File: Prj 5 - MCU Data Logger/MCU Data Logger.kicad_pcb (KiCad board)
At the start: 2 copper layers, 0 parts

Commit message: setup layout parameters
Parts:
- added BT1: Battery, Connector_PinHeader_2.54mm:PinHeader_1x02_P2.54mm_Vertical, F.Cu at (23.1, 45.1)
- added C1: 0.1u, Capacitor_SMD:C_0805_2012Metric, F.Cu at (44.8, 34.9)
- added C2: 0.1u, Capacitor_SMD:C_0805_2012Metric, F.Cu at (44.8, 37.9)
- added C3: 100n, Capacitor_SMD:C_0805_2012Metric, F.Cu at (44.8, 40.9)
- added C4: 22p, Capacitor_SMD:C_0805_2012Metric, F.Cu at (44.8, 43.9)
- added C5: 22p, Capacitor_SMD:C_0805_2012Metric, F.Cu at (44.8, 46.9)
- added D1: LED, LED_SMD:LED_0805_2012Metric, F.Cu at (49.3, 34.9)
- added D2: LED, LED_SMD:LED_0805_2012Metric, F.Cu at (49.3, 37.9)
- added H1: MountingHole, MountingHole:MountingHole_2.1mm, F.Cu at (23.6, 22.7)
- added H2: MountingHole, MountingHole:MountingHole_2.1mm, F.Cu at (23.6, 28.4)
- added H3: MountingHole, MountingHole:MountingHole_2.1mm, F.Cu at (23.6, 34.2)
- added H4: MountingHole, MountingHole:MountingHole_2.1mm, F.Cu at (23.6, 39.9)
- added J1: Conn_01x04_Pin, Connector_PinHeader_2.54mm:PinHeader_1x04_P2.54mm_Vertical, F.Cu at (60.4, 22.1)
- added J2: Conn_01x09_Pin, Connector_PinHeader_2.54mm:PinHeader_1x09_P2.54mm_Vertical, F.Cu at (55.8, 22.1)
- added J3: Conn_01x04_Pin, Connector_PinHeader_2.54mm:PinHeader_1x04_P2.54mm_Vertical, F.Cu at (65.1, 22.1)
- added J4: Conn_02x03_Odd_Even, Connector_PinHeader_2.54mm:PinHeader_2x03_P2.54mm_Vertical, F.Cu at (60.4, 34.4)
- added R1: 10k, Resistor_SMD:R_0805_2012Metric, F.Cu at (28.7, 21.3)
- added R2: 10k, Resistor_SMD:R_0805_2012Metric, F.Cu at (28.7, 24.2)
- added R3: 4.7K, Resistor_SMD:R_0805_2012Metric, F.Cu at (28.7, 27.2)
- added R4: 4.7K, Resistor_SMD:R_0805_2012Metric, F.Cu at (28.7, 30.1)
- added R5: 10K, Resistor_SMD:R_0805_2012Metric, F.Cu at (28.7, 33.1)
- added R6: 330R, Resistor_SMD:R_0805_2012Metric, F.Cu at (28.7, 36.0)
- added R7: 330R, Resistor_SMD:R_0805_2012Metric, F.Cu at (28.7, 39.0)
- added U1: 24LC1025, Package_SO:SOIC-8_5.23x5.23mm_P1.27mm, F.Cu at (36.1, 23.2)
- added U2: DS1337S+, #download:SOIC127P600X175-8N, F.Cu at (36.1, 48.3)
- added U3: 24LC1025, Package_SO:SOIC-8_5.23x5.23mm_P1.27mm, F.Cu at (36.1, 30.0)
- added U4: ATmega328P, Package_QFP:TQFP-32_7x7mm_P0.8mm, F.Cu at (36.7, 39.2)
- added Y1: 32.768KHz, Crystal:Crystal_SMD_5032-2Pin_5.0x3.2mm, F.Cu at (44.9, 22.2)
- added Y2: 16MHz, Crystal:Crystal_SMD_5032-2Pin_5.0x3.2mm, F.Cu at (44.9, 27.1)

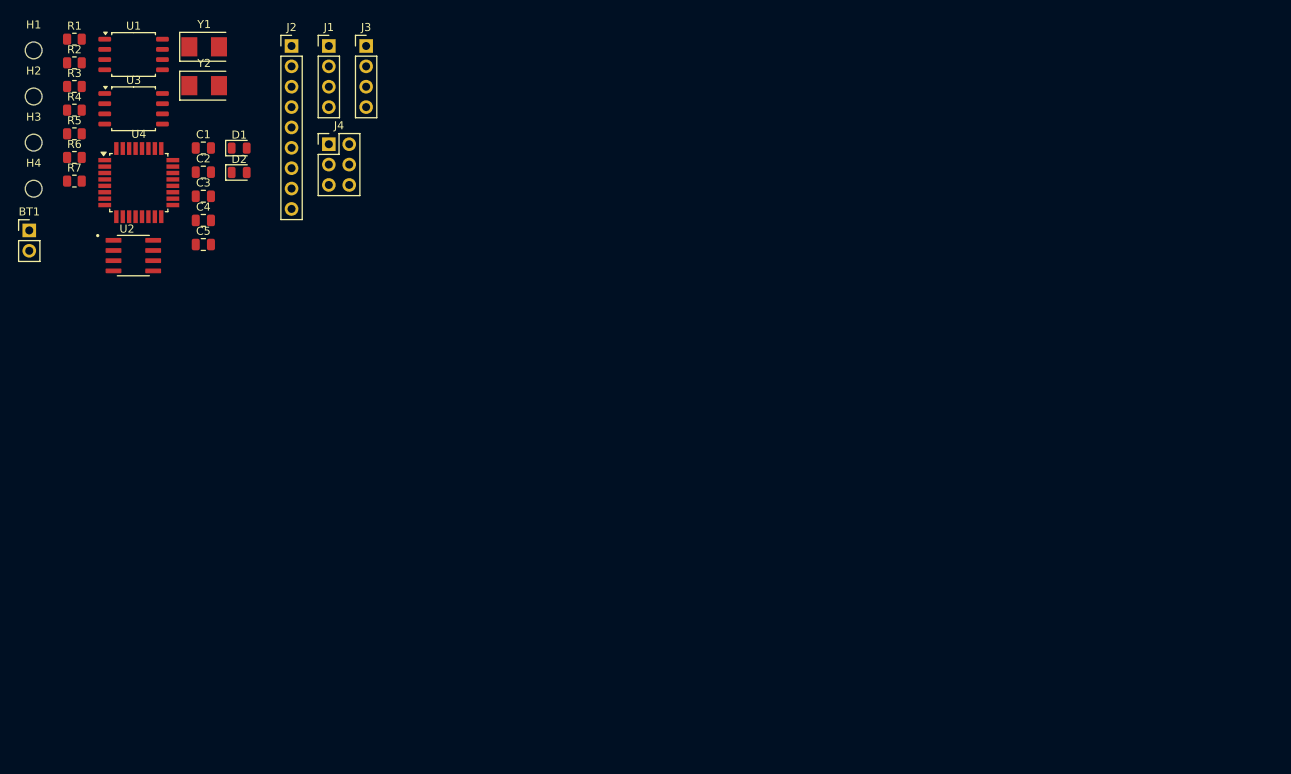
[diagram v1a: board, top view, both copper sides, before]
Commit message: distributed components and initial layout
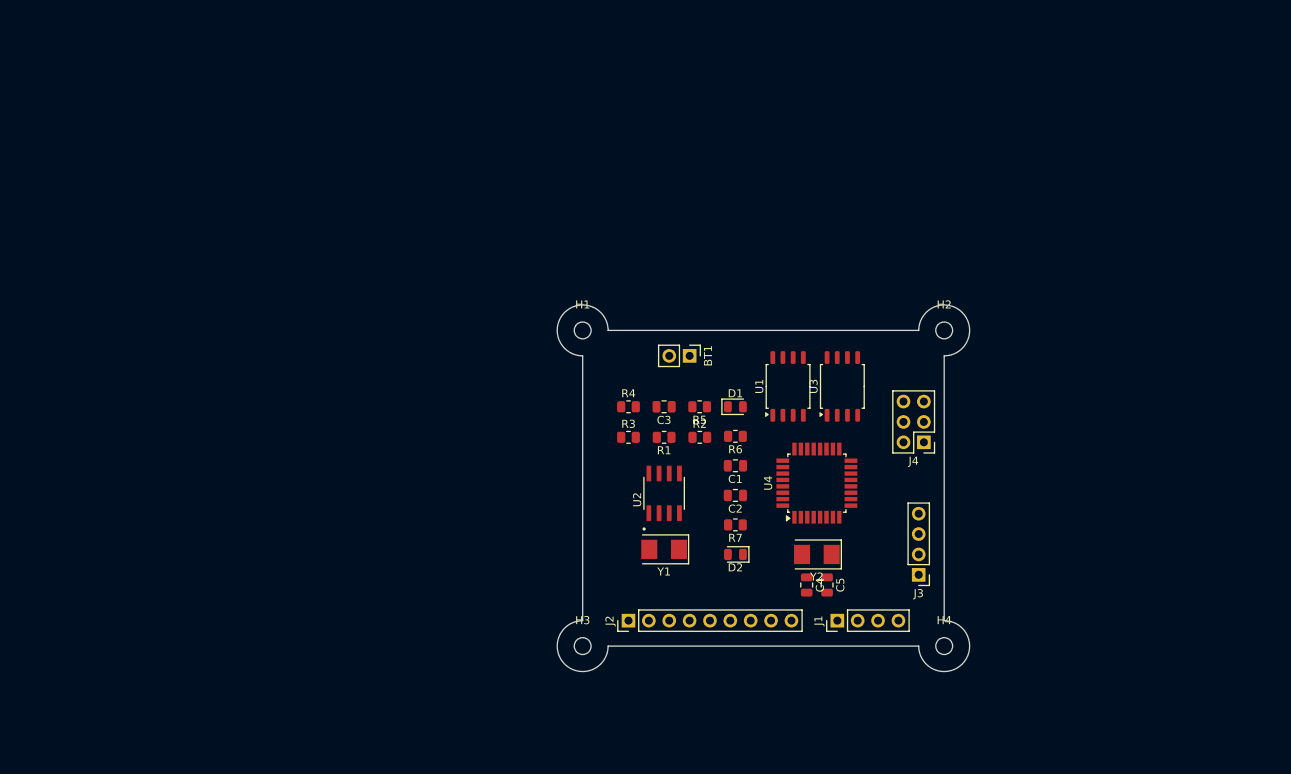
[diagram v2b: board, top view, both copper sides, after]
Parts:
- moved H4 127.1 mm to (137.2, 97.0)
- moved H2 117.2 mm to (137.2, 57.6)
- moved Y2 96.2 mm to (121.3, 85.5), turned to 180 degrees
- moved J1 95.7 mm to (123.9, 93.8), turned to 90 degrees
- moved J3 95.4 mm to (134.0, 88.1), turned to 180 degrees
- moved U3 94.9 mm to (124.5, 64.6), turned to 90 degrees
- moved R7 92.9 mm to (111.1, 81.9), turned to 180 degrees
- moved H3 92.9 mm to (92.1, 97.0)
- moved U4 92.5 mm to (121.3, 76.7), turned to 90 degrees
- moved U1 91.5 mm to (117.7, 64.6), turned to 90 degrees
- moved R2 90.9 mm to (106.7, 70.9)
- moved R6 89.5 mm to (111.1, 70.8), turned to 180 degrees
- moved R1 88.7 mm to (102.3, 70.9), turned to 180 degrees
- moved C5 88.6 mm to (122.6, 89.3), turned to -90 degrees
- moved C4 87.9 mm to (120.0, 89.3), turned to -90 degrees
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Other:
- board outline added: 51.4 x 45.7 mm

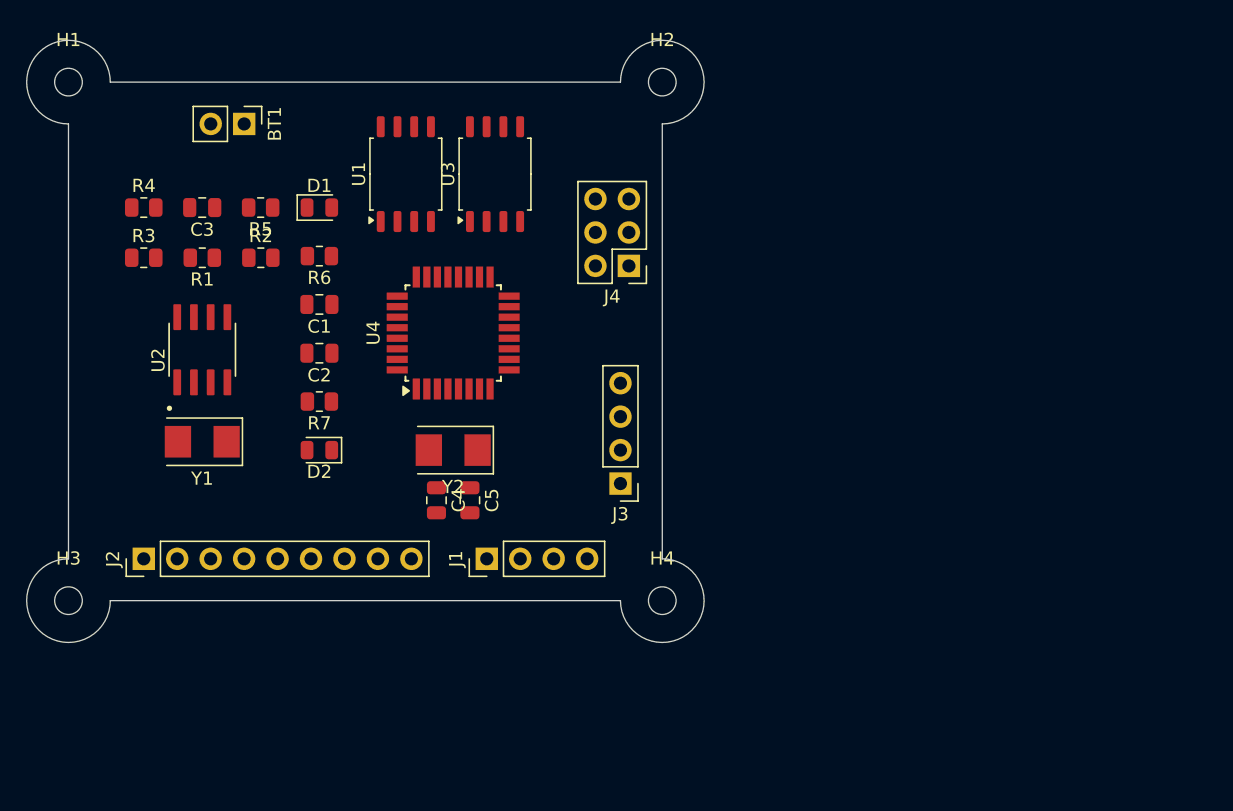
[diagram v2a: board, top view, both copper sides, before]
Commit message: Pausing, need fix on schecmatics
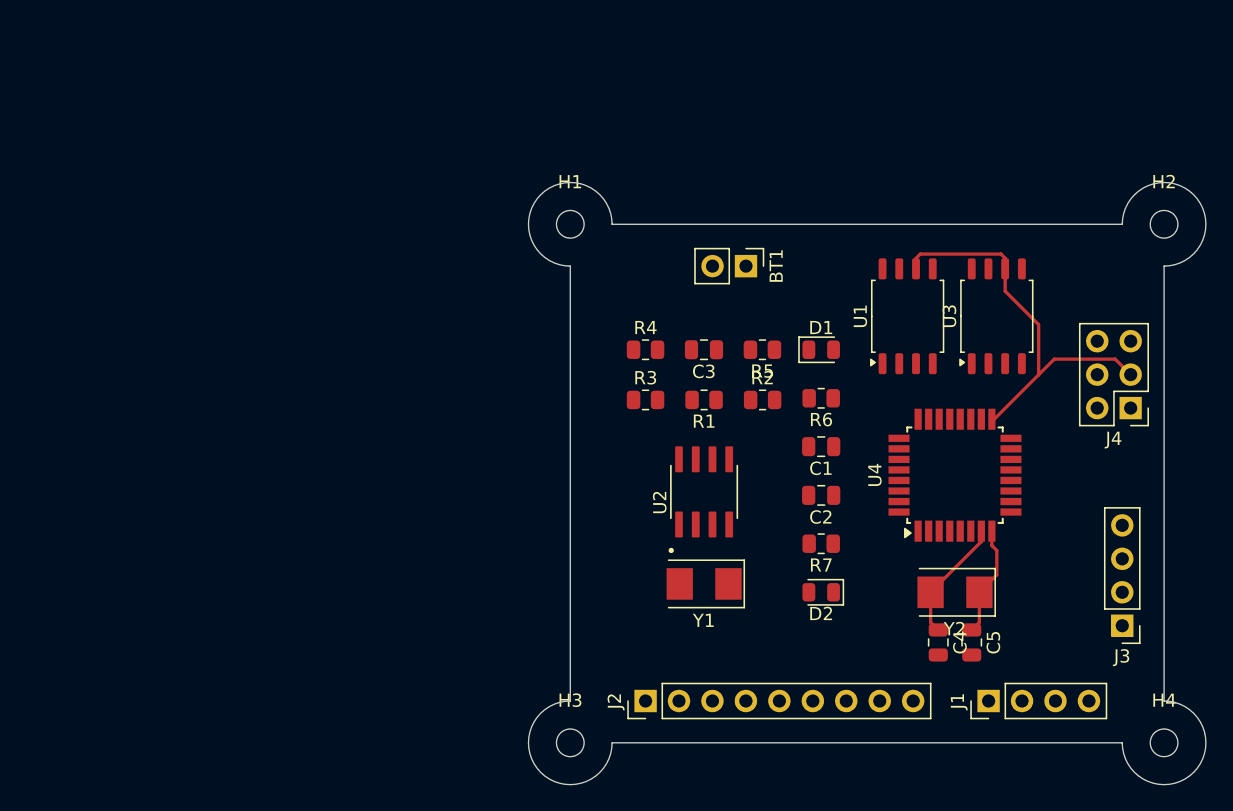
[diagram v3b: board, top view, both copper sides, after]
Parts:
- moved C1 39.6 mm to (149.2, 85.3)
- moved C5 39.6 mm to (160.7, 100.1)
- moved D1 39.6 mm to (149.2, 77.9)
- moved J1 39.6 mm to (162.0, 104.6)
- moved R2 39.6 mm to (144.8, 81.7)
- moved R7 39.6 mm to (149.2, 92.6)
- moved U1 39.6 mm to (155.8, 75.4)
- moved U3 39.6 mm to (162.6, 75.4)
- moved C2 39.6 mm to (149.2, 89.0)
- moved D2 39.6 mm to (149.2, 96.3)
- moved R6 39.6 mm to (149.2, 81.6)
- moved BT1 39.6 mm to (143.5, 71.6)
- moved C3 39.6 mm to (140.3, 77.9)
- moved C4 39.6 mm to (158.1, 100.1)
- moved H1 39.6 mm to (130.2, 68.4)
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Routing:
- net /SCK: track 0.00 -> 30.7 mm
- net Net-(U4-XTAL1/PB6): track 0.00 -> 9.33 mm
- net Net-(U4-XTAL2/PB7): track 0.00 -> 8.44 mm

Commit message: Completed routing, pending further improvements
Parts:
- D1: value LED -> LED1
- D2: value LED -> LED2
- moved D2 25.0 mm to (172.4, 86.8), turned to 90 degrees
- moved R7 21.0 mm to (169.4, 86.8), turned to -90 degrees
- moved J1 11.6 mm to (172.1, 98.9), turned to 180 degrees
- moved J3 11.6 mm to (162.0, 104.6), turned to 90 degrees
- moved U1 7.19 mm to (163.0, 75.4), turned to -90 degrees
- moved U3 6.35 mm to (156.2, 75.4), turned to -90 degrees
- moved C5 3.26 mm to (163.7, 99.0)
- moved Y2 2.62 mm to (161.8, 95.3)
- moved C4 2.22 mm to (160.0, 99.0)
- moved Y1 1.28 mm to (139.1, 95.6)
- turned C1 to 0 degrees
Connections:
- J1 pad 4: /SCK -> /SCL
- R3 pad 1: /SCK -> /SCL
- U1 pad 6: /SCK -> /SCL
- U2 pad 6: /SCK -> /SCL
- U3 pad 6: /SCK -> /SCL
- U4 pad 28: /SCK -> /SCL
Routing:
- net /BVcc: track 0.00 -> 215.6 mm, vias 0 -> 4
- net GND: track 0.00 -> 67.2 mm, vias 0 -> 9
- net /SCL: track 0.00 -> 66.2 mm, vias 0 -> 2
- net /SDA: track 0.00 -> 63.1 mm, vias 0 -> 2
- net /RESET: track 0.00 -> 47.2 mm
- net /D5: track 0.00 -> 38.8 mm, vias 0 -> 1
- net /D6: track 0.00 -> 37.9 mm, vias 0 -> 1
- net /D7: track 0.00 -> 37.1 mm, vias 0 -> 1
- net /D8: track 0.00 -> 36.4 mm, vias 0 -> 1
- net /D2: track 0.00 -> 30.3 mm, vias 0 -> 1
- net /TX: track 0.00 -> 30.2 mm
- net /RX: track 0.00 -> 30.2 mm
- net /D3: track 0.00 -> 27.5 mm, vias 0 -> 1
- net /D4: track 0.00 -> 25.7 mm, vias 0 -> 1
- net Net-(U2-~{INTA}): track 0.00 -> 14.6 mm
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- added copper zone on B.Cu, net GND

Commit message: v0.1 Complete, ready for manuf
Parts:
- added REF**: KiCad-Logo_6mm_SilkScreen, Symbol:KiCad-Logo_6mm_SilkScreen, B.Cu at (152.7, 73.7)
- renumbered BT1 to Battery
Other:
- board text added: "${PROJECT_NAME}"
- board text added: "+"
- board text added: "-"
- board text added: "D2"
- board text added: "D3"
- board text added: "D4"
- board text added: "D5"
- board text added: "D6"
- board text added: "D7"
- board text added: "D8"
- board text added: "GND"
- board text added: "ICSP"
- board text added: "MISO"
- board text added: "MOSI"
- board text added: "RST"
- board text added: "Rx"
- board text added: "SCK"
- board text added: "SCL"
- board text added: "SDA"
- board text added: "Tx"
- board text added: "V${BOARD_VERSION}.${REVISION}"
- board text added: "Vcc"
